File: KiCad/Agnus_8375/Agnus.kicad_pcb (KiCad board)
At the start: 4 copper layers, 30.2 x 30.2 mm, 27 parts, among them J1 Conn_01x21, J2 Conn_01x21, J3 Conn_01x21, J4 Conn_01x21, U1 10M02SCU169C8G, U2 LM1117-3.3, U3 SN74CBTD16210, U4 SN74CBTD16210, U5 SN74CBTD16210, U6 SN74CBTD16210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

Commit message: Updated routing, unused CLK pins to GND, added more caps
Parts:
- added C10: 0.01uF, Capacitor_SMD:C_0603_1608Metric_Pad1.05x0.95mm_HandSolder, F.Cu at (152.8, 81.9)
- added C4: 0.01uF, Capacitor_SMD:C_0603_1608Metric_Pad1.05x0.95mm_HandSolder, F.Cu at (147.6, 72.7)
- added C6: 0.01uF, Capacitor_SMD:C_0603_1608Metric_Pad1.05x0.95mm_HandSolder, F.Cu at (137.3, 81.9)
- added C7: 0.01uF, Capacitor_SMD:C_0603_1608Metric_Pad1.05x0.95mm_HandSolder, F.Cu at (143.7, 86.7)
- C11: renamed from C6; value 0.1uF -> 0.01uF
- C12: renamed from C5; value 0.1uF -> 0.01uF
- C13: renamed from C4; value 0.1uF -> 0.01uF
- C14: renamed from C11; value 0.1uF -> 0.01uF
- C15: renamed from C12; value 0.1uF -> 0.01uF
- C16: renamed from C13; value 0.1uF -> 0.01uF
- C17: renamed from C14; value 0.1uF -> 0.01uF
- renumbered C8 to C5, C9 to C8, C7 to C9, RN2 to RN1, RN1 to RN2
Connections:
- RN2 pad 3: JTAGEN -> Net-(RN2-Pad3)
- RN2 pad 6: 3V3 -> Net-(RN2-Pad6)
- U1 pad E1: JTAGEN -> Net-(U1-PadE1)
- U1 pad E2: JTAGEN -> Net-(U1-PadE2)
- U1 pad E3: JTAGEN -> Net-(U1-PadE3)
- U1 pad E4: JTAGEN -> Net-(U1-PadE4)
- U1 pad E5: JTAGEN -> Net-(U1-PadE5)
- U1 pad G10: Net-(U1-PadG10) -> GND
- U1 pad G9: Net-(U1-PadG9) -> GND
- U1 pad H5: Net-(U1-PadH5) -> GND
- U1 pad H6: Net-(U1-PadH6) -> GND
- U1 pad L3: Net-(U1-PadL3) -> GND
- U1 pad N2: Net-(U1-PadN2) -> GND
- U1 pad N3: Net-(U1-PadN3) -> GND
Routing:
- net GND: track 166.3 -> 199.3 mm, vias 28 -> 30
- net JTAGEN: track 14.5 -> 0.00 mm
- net 3V3: track 189.2 -> 194.6 mm
- net TCK: track 21.6 -> 23.6 mm
- net TMS: track 13.3 -> 15.1 mm
- net CCK: track 7.01 -> 6.43 mm
- net 14M: track 8.04 -> 7.50 mm

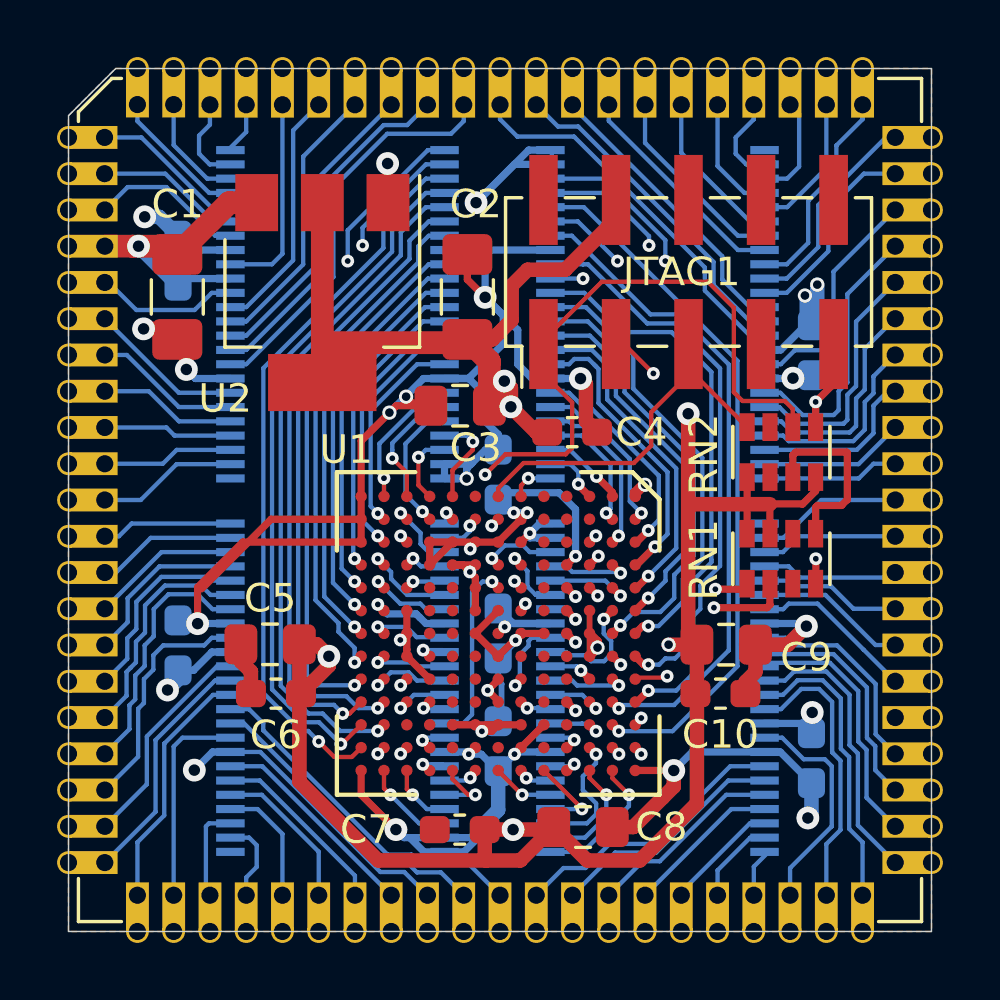
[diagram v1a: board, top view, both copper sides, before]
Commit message: VCC/GND improvements, added 3V3 filled zone, added testpad with conn to E1
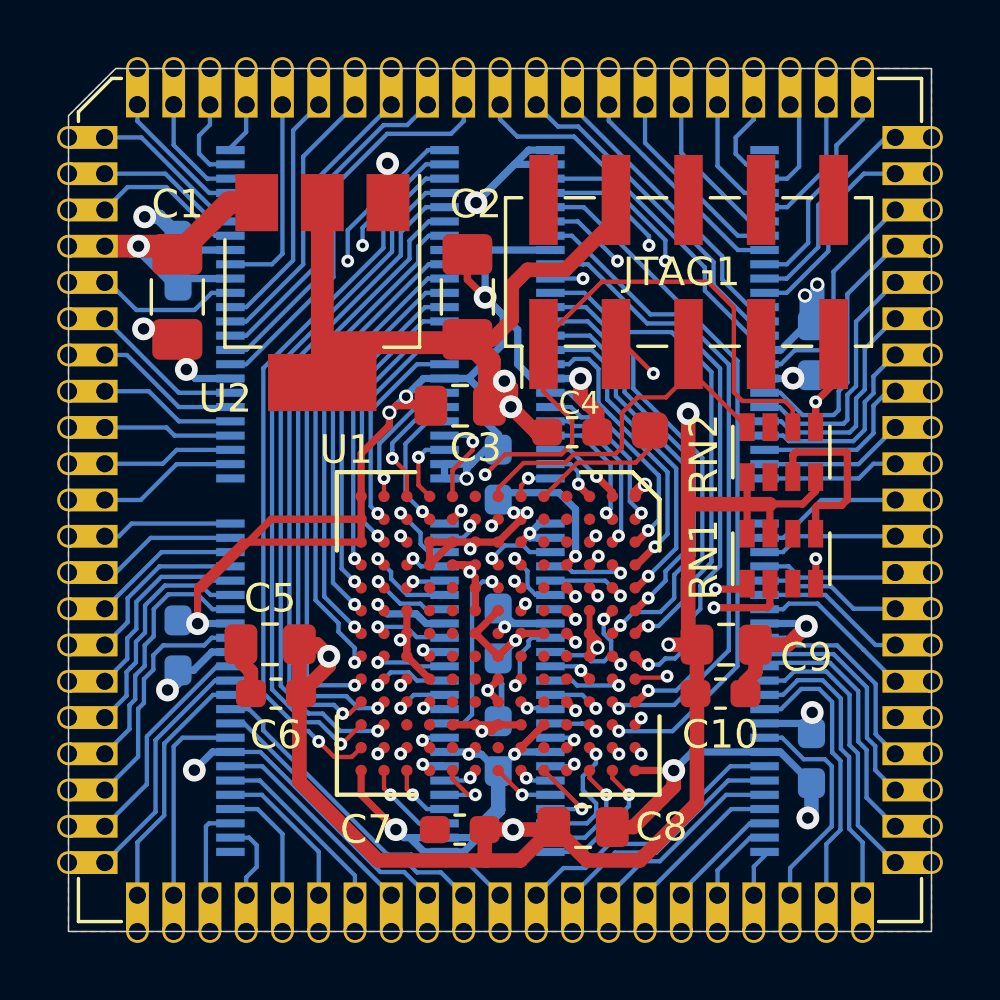
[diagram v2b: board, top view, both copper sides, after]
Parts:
- added J5: Conn_01x01, Agnus:PinHeader_1x01_1.27x1.27mm_SMD, F.Cu at (150.4, 72.7)
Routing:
- net 3V3: track 194.6 -> 202.4 mm
- net Net-(J5-Pad1): track 0.00 -> 5.04 mm
- net GND: track 199.3 -> 202.2 mm
- net VCC: track 20.2 -> 22.0 mm
- net REGEN_FPGA: track 0.71 -> 1.31 mm
- added copper zone on VCC.Cu, net 3V3

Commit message: cleanup and improved routing, added testpin/debugpin with conn to L11
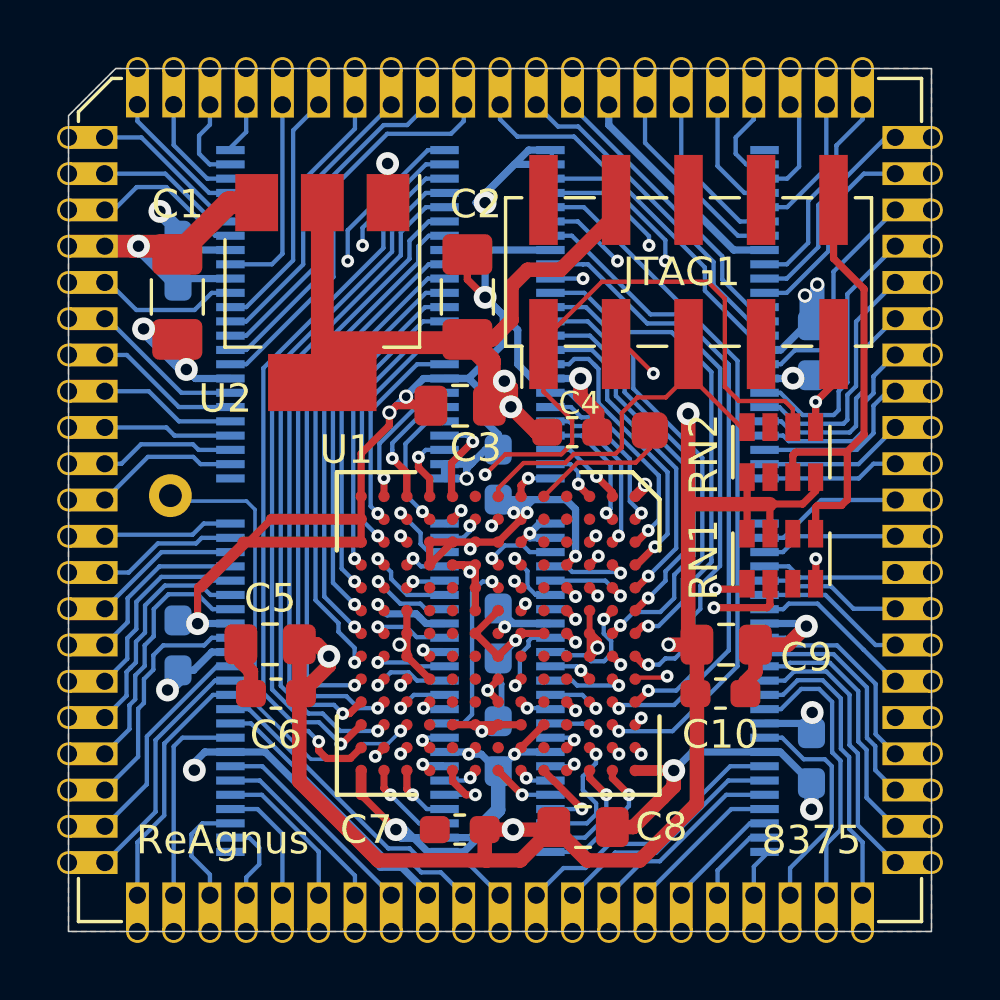
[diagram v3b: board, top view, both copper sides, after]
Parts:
- added J6: Conn_01x01, Agnus:PinHeader_1x01_1.5x1.5mm_Vertical, F.Cu at (133.6, 75.0)
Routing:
- net GND: track 202.2 -> 220.6 mm
- net Net-(J6-Pad1): track 0.00 -> 16.9 mm, vias 0 -> 1
- net 3V3: track 202.4 -> 201.3 mm
- net A20: track 3.29 -> 3.93 mm
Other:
- rule trace_min: 0.1524 -> 0.127
- board text added: "8375"
- board text added: "ReAgnus"

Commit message: added 10k pull-up on JTAG pin 8
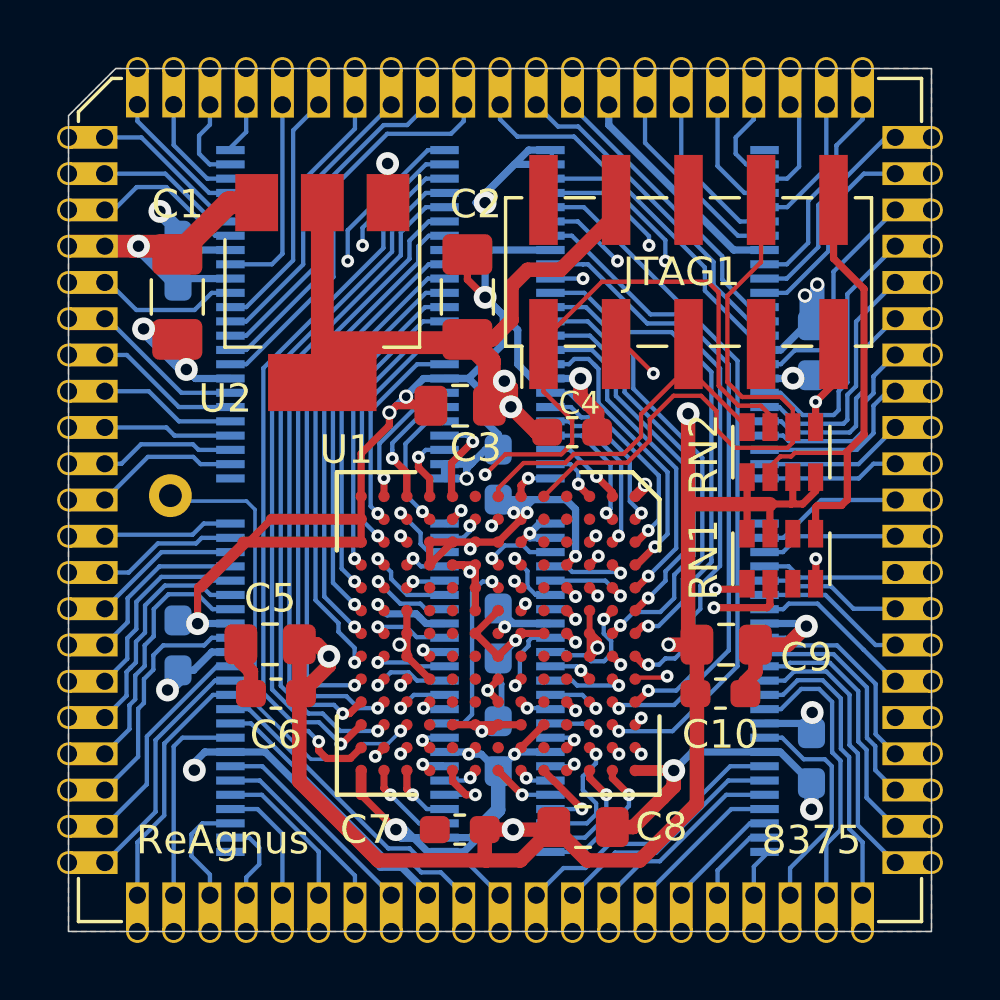
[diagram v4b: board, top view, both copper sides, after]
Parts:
- removed J5: Conn_01x01, Agnus:PinHeader_1x01_1.27x1.27mm_SMD
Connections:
- JTAG1 pad 8: Net-(JTAG1-Pad8) -> nNTSC
- RN2 pad 2: TCK -> nNTSC
- RN2 pad 3: Net-(RN2-Pad3) -> TCK
- RN2 pad 6: Net-(RN2-Pad6) -> GND
- RN2 pad 7: GND -> 3V3
- U1 pad E1: Net-(J5-Pad1) -> nNTSC
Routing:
- net nNTSC: track 0.00 -> 22.5 mm
- net Net-(J5-Pad1): track 5.04 -> 0.00 mm
- net 3V3: track 201.3 -> 202.3 mm
- net TCK: track 23.6 -> 22.8 mm
- net GND: track 220.6 -> 221.2 mm
- net TMS: track 15.2 -> 14.7 mm

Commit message: Removed castellated holes, adjusted size and board edges, changed to 0.4/0.2mm vias, centered vias in BGA-pads.
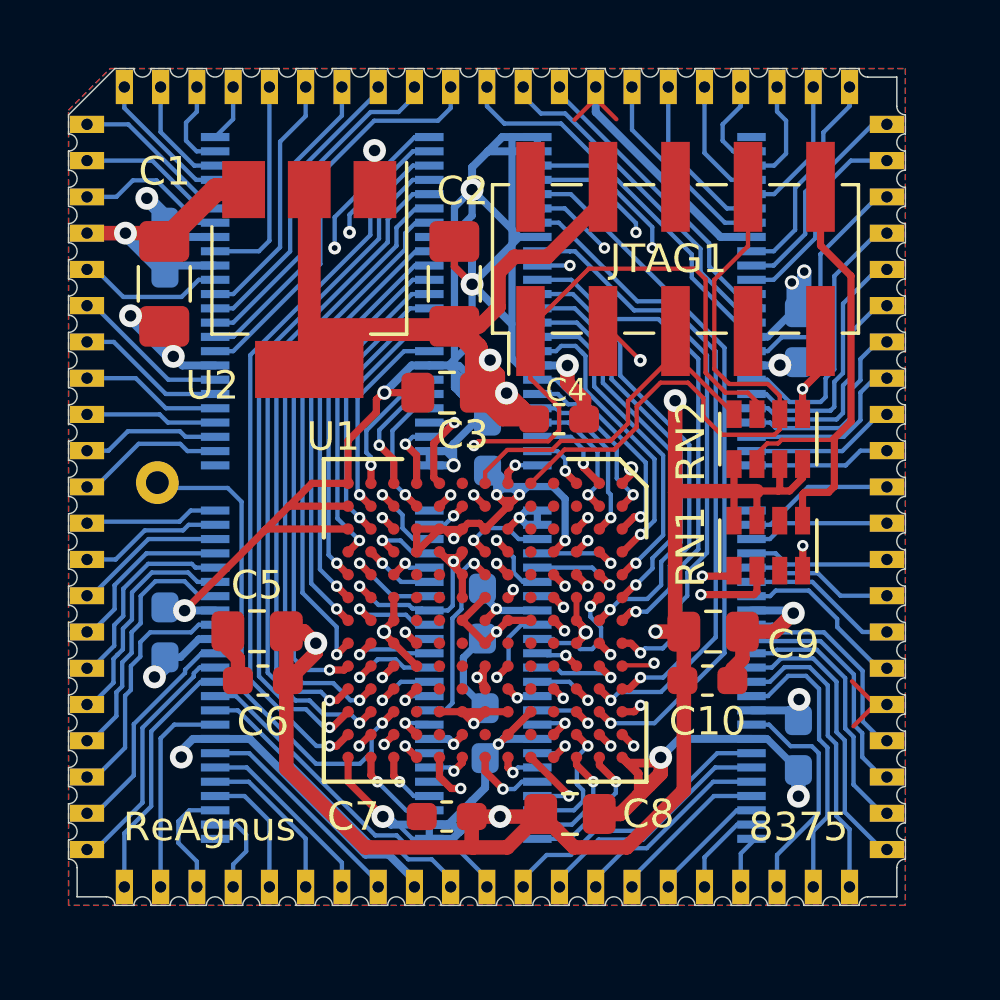
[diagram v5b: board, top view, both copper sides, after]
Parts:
- removed J1, J2, J3, J4: Conn_01x21, Agnus:PinHeader_1x21_P1.27mm_Vertical
- moved C13 1.08 mm to (144.7, 73.2)
- moved C12 0.89 mm to (144.5, 79.1)
- moved U4 0.70 mm to (138.9, 68.2)
- moved U6 0.70 mm to (138.9, 81.2)
- moved C1 0.65 mm to (133.4, 67.5)
- moved C10 0.65 mm to (152.4, 81.4)
- moved C11 0.65 mm to (144.6, 83.3)
- moved C14 0.65 mm to (133.4, 66.3)
- moved C16 0.65 mm to (155.6, 69.4)
- moved C17 0.65 mm to (155.6, 83.7)
- moved C2 0.65 mm to (143.5, 67.5)
- moved C3 0.65 mm to (143.3, 71.4)
- moved C4 0.65 mm to (147.2, 72.3)
- moved C6 0.65 mm to (136.8, 81.4)
- moved C7 0.65 mm to (143.2, 86.2)
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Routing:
- net 3V3: track 202.3 -> 212.2 mm
- net DRD1_FPGA: track 22.3 -> 21.3 mm
- net RGA8_FPGA: track 1.53 -> 2.40 mm
- net RGA6_FPGA: track 3.31 -> 2.48 mm
- net GND: track 221.2 -> 220.4 mm, vias 30 -> 29
- net Net-(J6-Pad1): track 16.9 -> 17.7 mm
- net DRD7_FPGA: track 18.8 -> 18.2 mm
- net BLISS_FPGA: track 4.43 -> 3.86 mm
- net TDI: track 19.5 -> 20.0 mm
- net RGA2_FPGA: track 2.70 -> 3.21 mm
- net RGA1_FPGA: track 2.95 -> 3.46 mm
- net UDS_FPGA: track 2.03 -> 2.54 mm
- net DRA9_FPGA: track 2.78 -> 3.29 mm
- net A2_FPGA: track 2.41 -> 2.91 mm
- net CASU_FPGA: track 2.10 -> 2.60 mm
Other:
- board size 30.2 x 30.2 mm -> 29.3 x 29.3 mm
- net class Default: via_dia 0.45 -> 0.4
- rule via_min_size: 0.45 -> 0.4

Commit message: Reassigned A7_FPGA, A8_FPGA to D1 and C1, reassigned pad B1 as debug-pin to JTAG free pin 7 (NC)
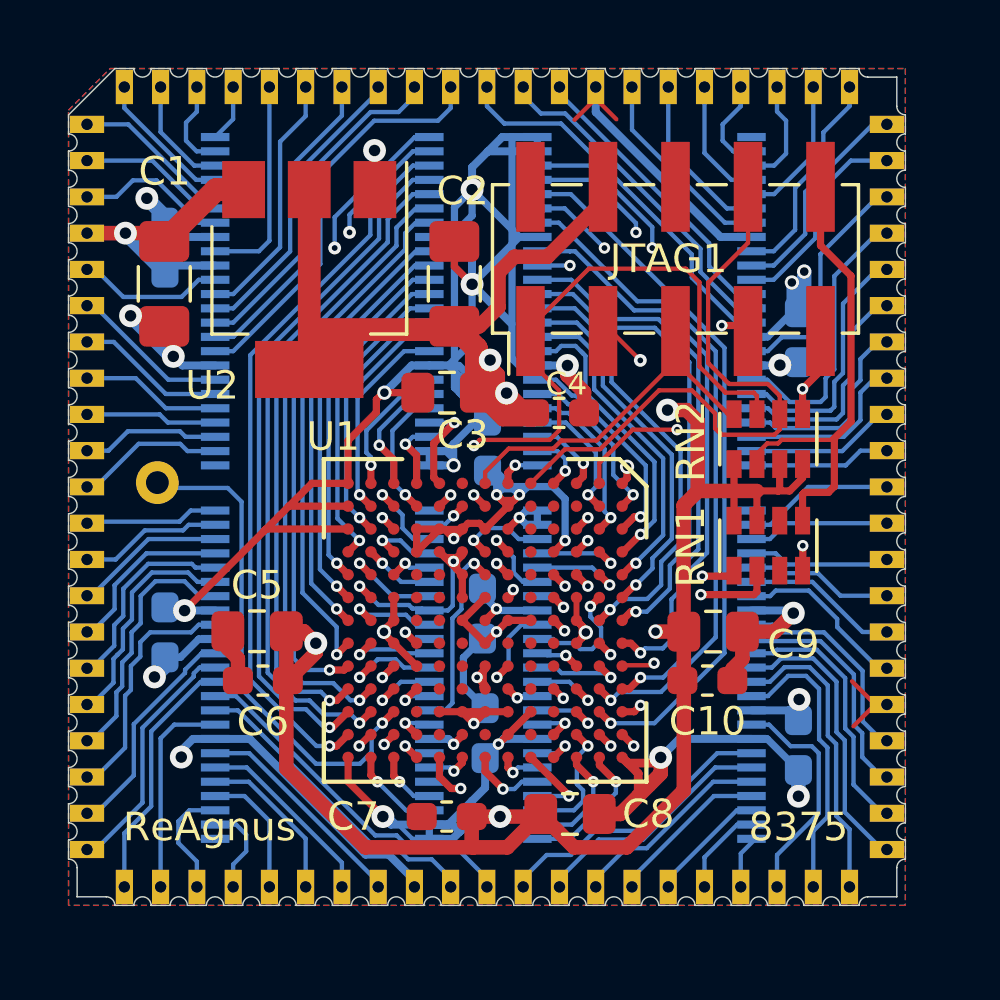
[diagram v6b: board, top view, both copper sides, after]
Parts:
- moved C4 0.22 mm to (147.2, 72.1)
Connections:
- JTAG1 pad 7: Net-(JTAG1-Pad7) -> DEBUG_PIN
- U1 pad B1: A8_FPGA -> DEBUG_PIN
- U1 pad C1: A7_FPGA -> A8_FPGA
- U1 pad D1: Net-(U1-PadD1) -> A7_FPGA
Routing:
- net DEBUG_PIN: track 0.00 -> 9.70 mm, vias 0 -> 2
- net A14_FPGA: track 15.7 -> 16.7 mm
- net nNTSC: track 22.5 -> 22.0 mm
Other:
- rule trace_min: 0.127 -> 0.1524
